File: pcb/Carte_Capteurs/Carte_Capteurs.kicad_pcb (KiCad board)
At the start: 2 copper layers, 129.9 x 60 mm, 0 parts

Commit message: demarrage carte capteurs
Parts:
- added Logo1: LOGO, Insa:insa-image, F.Cu at (210.3, 88.9)
- added U1: FRDM-KL25Z, Insa:FRDM-KL25Z, B.Cu at (149.9, 104.1)

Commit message: version d'echange
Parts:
- added C1: 100nF, Capacitor_SMD:C_1206_3216Metric_Pad1.42x1.75mm_HandSolder, F.Cu at (131.2, 88.8)
- added C2: 100µF, Capacitor_THT:CP_Radial_D6.3mm_P2.50mm, F.Cu at (173.0, 110.4)
- added C3: 100µF, Capacitor_THT:CP_Radial_D6.3mm_P2.50mm, F.Cu at (180.0, 110.4)
- added C4: 100nF, Capacitor_SMD:C_1206_3216Metric_Pad1.42x1.75mm_HandSolder, F.Cu at (131.2, 91.1)
- added D1: LED, LED_THT:LED_D3.0mm, F.Cu at (140.9, 116.2)
- added J10: Conn_01x05, Connector_PinHeader_2.54mm:PinHeader_1x05_P2.54mm_Horizontal, F.Cu at (160.1, 94.5)
- added J11: Conn_01x04, Connector_PinHeader_2.54mm:PinHeader_1x04_P2.54mm_Horizontal, F.Cu at (147.7, 108.3)
- added J12: Conn_01x04, Connector_PinHeader_2.54mm:PinHeader_1x04_P2.54mm_Horizontal, F.Cu at (160.1, 108.3)
- added J5: Conn_02x07_Odd_Even, Connector_PinHeader_2.54mm:PinHeader_2x07_P2.54mm_Vertical, F.Cu at (141.5, 94.5)
- added J6: Molex KK 254, Connector_Molex:Molex_KK-254_AE-6410-04A_1x04_P2.54mm_Vertical, F.Cu at (172.5, 96.2)
- added J7: Samtec FTS-105-01-L-DV, Connector_PinHeader_1.27mm:PinHeader_2x05_P1.27mm_Vertical, F.Cu at (172.3, 100.7)
- added J8: Samtec FTS-105-01-L-DV, Connector_PinHeader_1.27mm:PinHeader_2x05_P1.27mm_Vertical, F.Cu at (176.8, 100.7)
- added J9: Conn_01x05, Connector_PinHeader_2.54mm:PinHeader_1x05_P2.54mm_Horizontal, F.Cu at (147.7, 94.5)
- added R1: R, Resistor_SMD:R_1206_3216Metric_Pad1.42x1.75mm_HandSolder, F.Cu at (142.2, 112.8)
- added U2: XBee, Insa:Xbee3, F.Cu at (116.1, 101.7)
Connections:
- U1 pad 3.16: (no net) -> +BATT
- U1 pad 3.4: (no net) -> /PWR_LED

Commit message: sauvegarde intermediaire
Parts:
- added C10: 100nF, Capacitor_SMD:C_1206_3216Metric_Pad1.42x1.75mm_HandSolder, F.Cu at (108.0, 113.7)
- added C11: 100nF, Capacitor_SMD:C_1206_3216Metric_Pad1.42x1.75mm_HandSolder, F.Cu at (197.5, 113.7)
- added C5: 100nF, Capacitor_SMD:C_1206_3216Metric_Pad1.42x1.75mm_HandSolder, F.Cu at (184.2, 85.1)
- added C6: 100nF, Capacitor_SMD:C_1206_3216Metric_Pad1.42x1.75mm_HandSolder, F.Cu at (123.2, 97.8)
- added C7: 100nF, Capacitor_SMD:C_1206_3216Metric_Pad1.42x1.75mm_HandSolder, F.Cu at (123.2, 90.4)
- added C8: 100nF, Capacitor_SMD:C_1206_3216Metric_Pad1.42x1.75mm_HandSolder, F.Cu at (118.7, 80.0)
- added C9: 100nF, Capacitor_SMD:C_1206_3216Metric_Pad1.42x1.75mm_HandSolder, F.Cu at (131.4, 80.0)
- added J13: Conn_01x02, Connector_PinHeader_2.54mm:PinHeader_1x02_P2.54mm_Vertical, F.Cu at (115.6, 106.7)
- added Q1: NTR3C21NZT1G, Package_TO_SOT_SMD:SOT-23, F.Cu at (119.4, 111.8)
- added R3: 10K, Resistor_SMD:R_1206_3216Metric_Pad1.42x1.75mm_HandSolder, F.Cu at (109.9, 90.2)
- added R4: 10K, Resistor_SMD:R_1206_3216Metric_Pad1.42x1.75mm_HandSolder, F.Cu at (107.3, 100.3)
- added R5: 100R, Resistor_SMD:R_1206_3216Metric_Pad1.42x1.75mm_HandSolder, F.Cu at (123.2, 111.1)
- added RN1: 100R, Resistor_SMD:R_Array_Convex_4x1206, F.Cu at (142.2, 86.4)
- added RN2: 100R, Resistor_SMD:R_Array_Convex_4x1206, F.Cu at (142.2, 94.0)
- added RN3: 10K, Resistor_SMD:R_Array_Convex_4x1206, F.Cu at (167.6, 84.2)
- added SW1: SMR8016C-1, Insa:Nidec_Copal_SMR-8016C, F.Cu at (167.6, 92.1)
- added SW2: Reset, Button_Switch_THT:SW_PUSH_6mm_H4.3mm, F.Cu at (108.6, 83.2)
- added SW3: USER1, Button_Switch_THT:SW_PUSH_6mm_H4.3mm, F.Cu at (106.0, 93.3)
- added SW4: USER2, Button_Switch_THT:SW_PUSH_6mm_H4.3mm, F.Cu at (103.5, 103.5)
- added U3: HDSP-7501, Display_7Segment:HDSP-A151, F.Cu at (156.8, 94.6)
- added U4: TCL6C598, Package_SO:TSSOP-16_4.4x5mm_P0.65mm, F.Cu at (134.6, 92.7)
- J10, J9: value Conn_01x05 -> DF3A-5P-2DS; footprint Connector_PinHeader_2.54mm:PinHeader_1x05_P2.54mm_Horizontal -> Insa:DF3A-5P-2DS
- J11, J12: value Conn_01x04 -> DF3A-4P-2DS; footprint Connector_PinHeader_2.54mm:PinHeader_1x04_P2.54mm_Horizontal -> Insa:DF3A-4P-2DS
- moved Logo1 116.4 mm to (96.4, 113.0), turned to 270 degrees
- moved U2 77.0 mm to (190.5, 81.9)
- moved C4 73.5 mm to (203.2, 105.8), turned to 270 degrees
- moved C1 63.2 mm to (185.4, 121.3), turned to 180 degrees
- moved J8 57.3 mm to (119.6, 97.2), turned to 270 degrees
- moved J7 53.8 mm to (119.6, 89.8), turned to 270 degrees
- moved J9 46.8 mm to (107.3, 118.1)
- moved J11 44.2 mm to (118.1, 75.6), turned to 180 degrees
- moved J12 44.0 mm to (130.8, 75.6), turned to 180 degrees
- moved J10 43.6 mm to (196.8, 118.1)
- moved C3 18.4 mm to (197.5, 104.8), turned to 270 degrees
- moved C2 14.6 mm to (186.7, 115.6), turned to 180 degrees
- moved J5 14.6 mm to (145.4, 108.6), turned to 90 degrees
- moved J6 14.4 mm to (181.6, 107.3)
- moved D1 12.5 mm to (130.8, 108.7), turned to 90 degrees
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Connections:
- J10 pad 1: (no net) -> /ENC_INDEX2
- J10 pad 2: (no net) -> +3V3
- J10 pad 3: (no net) -> /ENC_SIG_A2
- J10 pad 4: (no net) -> /ENC_SIG_B2
- J10 pad 5: (no net) -> GND
- J11 pad 1: (no net) -> +3V3
- J11 pad 2: (no net) -> /SENS_SDA1
- J11 pad 3: (no net) -> GND
- J11 pad 4: (no net) -> /SENS_SCL1
- J12 pad 1: (no net) -> +3V3
- J12 pad 2: (no net) -> /SENS_SDA2
- J12 pad 3: (no net) -> GND
- J12 pad 4: (no net) -> /SENS_SCL2
- J5 pad 1: (no net) -> /DISABLE_MOT_R
- J5 pad 10: (no net) -> /PWM_MOT_R_2
- J5 pad 12: (no net) -> /PWM_MOT_L_1
- J5 pad 14: (no net) -> /PWM_MOT_L_2
- J5 pad 2: (no net) -> /SERVO_PWM
- J5 pad 3: (no net) -> /DISABLE_MOT_L
- J5 pad 4: (no net) -> /FEEDBACK_MOT_R
- J5 pad 6: (no net) -> /FEEDBACK_MOT_L
- J5 pad 8: (no net) -> /PWM_MOT_R_1
- J7 pad 1: (no net) -> GND
- J7 pad 10: (no net) -> GND
- J7 pad 2: (no net) -> /CCD_AD0
- J7 pad 3: (no net) -> GND
- J7 pad 4: (no net) -> /CCD_SI0
- J7 pad 5: (no net) -> GND
- J7 pad 6: (no net) -> /CCD_CLK0
- J7 pad 7: (no net) -> GND
- J7 pad 8: (no net) -> +3V3
- J7 pad 9: (no net) -> GND
- J8 pad 1: (no net) -> GND
- J8 pad 10: (no net) -> GND
- J8 pad 2: (no net) -> /CCD_AD1
- J8 pad 3: (no net) -> GND
- J8 pad 4: (no net) -> /CCD_SI1
- J8 pad 5: (no net) -> GND
- J8 pad 6: (no net) -> /CCD_CLK1
- J8 pad 7: (no net) -> GND
- J8 pad 8: (no net) -> +3V3
- J8 pad 9: (no net) -> GND
- J9 pad 1: (no net) -> /ENC_INDEX1
- J9 pad 2: (no net) -> +3V3
- J9 pad 3: (no net) -> /ENC_SIG_A1
- J9 pad 4: (no net) -> /ENC_SIG_B1
- J9 pad 5: (no net) -> GND
- U1 pad 1.1: (no net) -> /DISABLE_MOT_R
- U1 pad 1.10: (no net) -> /PWM_MOT_R_1
- U1 pad 1.11: (no net) -> /DISP_SIN
- U1 pad 1.12: (no net) -> /PWM_MOT_R_2
- U1 pad 1.13: (no net) -> /DISP_LATCH
- U1 pad 1.14: (no net) -> /PWM_MOT_L_1
- U1 pad 1.16: (no net) -> /PWM_MOT_L_2
- U1 pad 1.2: (no net) -> /ENC_SIG_B1
- U1 pad 1.3: (no net) -> /DISABLE_MOT_L
- U1 pad 1.4: (no net) -> /ENC_SIG_B2
- U1 pad 1.6: (no net) -> /ENC_INDEX1
- U1 pad 1.8: (no net) -> /SERVO_PWM
- U1 pad 1.9: (no net) -> /DISP_CLK
- U1 pad 2.1: (no net) -> /CAM_LED
- U1 pad 2.10: (no net) -> /SW_USER1
- U1 pad 2.12: (no net) -> /SW_USER2
- U1 pad 2.14: (no net) -> GND
- U1 pad 2.17: (no net) -> /FEEDBACK_MOT_L
- U1 pad 2.18: (no net) -> /SENS_SCL1
- U1 pad 2.2: (no net) -> /ENC_INDEX2
- U1 pad 2.20: (no net) -> /SENS_SDA1
- U1 pad 2.4: (no net) -> /FEEDBACK_MOT_R
- U1 pad 3.1: (no net) -> /CCD_SI0
- U1 pad 3.11: (no net) -> /ROT_SW_2
- U1 pad 3.12: (no net) -> GND
- U1 pad 3.13: (no net) -> /ROT_SW_4
- U1 pad 3.14: (no net) -> GND
- U1 pad 3.15: (no net) -> /ROT_SW_8
- U1 pad 3.3: (no net) -> /CCD_CLK0
- U1 pad 3.5: (no net) -> /CCD_SI1
- U1 pad 3.6: (no net) -> /RESET
- U1 pad 3.7: (no net) -> /CCD_CLK1
- U1 pad 3.9: (no net) -> /ROT_SW_1
- U1 pad 4.10: (no net) -> /CCD_AD0
- U1 pad 4.12: (no net) -> /CCD_AD1
- U1 pad 4.2: (no net) -> /SENS_SCL2
- U1 pad 4.4: (no net) -> /SENS_SDA2
- U1 pad 4.5: (no net) -> /USART_TX
- U1 pad 4.6: (no net) -> /ENC_SIG_A1
- U1 pad 4.7: (no net) -> /USART_RX
- U1 pad 4.8: (no net) -> /ENC_SIG_A2
- U2 pad 2: (no net) -> /USART_RX
- U2 pad 3: (no net) -> /USART_TX
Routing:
- net GND: track 0.00 -> 341.3 mm
- net +3V3: track 0.00 -> 227.5 mm, vias 0 -> 3
- net +BATT: track 0.00 -> 100.1 mm
- net /ENC_INDEX1: track 0.00 -> 77.9 mm, vias 0 -> 1
- net /ENC_SIG_B1: track 0.00 -> 77.1 mm, vias 0 -> 1
- net /ENC_INDEX2: track 0.00 -> 52.3 mm
- net /DISABLE_MOT_R: track 0.00 -> 44.9 mm, vias 0 -> 2
- net /PWM_MOT_L_1: track 0.00 -> 37.3 mm, vias 0 -> 1
- net /PWM_MOT_L_2: track 0.00 -> 36.3 mm
- net /ENC_SIG_B2: track 0.00 -> 35.9 mm
- net /DISABLE_MOT_L: track 0.00 -> 34.1 mm, vias 0 -> 1
- net /SERVO_PWM: track 0.00 -> 33.4 mm, vias 0 -> 1
- net Net-(RN2-Pad2): track 0.00 -> 27.0 mm, vias 0 -> 1
- net /PWM_MOT_R_1: track 0.00 -> 26.7 mm
- net /ROT_SW_2: track 0.00 -> 25.0 mm
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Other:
- outline, holes or cut-outs redrawn
- net class Default: trace_width 0.25 -> 0.35; via_dia 0.8 -> 0.7
- net class Power added: clearance 0.2, trace_width 0.5, via_dia 1, via_drill 0.6

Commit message: Cartes terminées
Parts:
- added R6: 4.7K, Resistor_SMD:R_1206_3216Metric_Pad1.42x1.75mm_HandSolder, B.Cu at (132.1, 73.0)
- added R7: 4.7K, Resistor_SMD:R_1206_3216Metric_Pad1.42x1.75mm_HandSolder, B.Cu at (132.1, 70.5)
- added R8: 4.7K, Resistor_SMD:R_1206_3216Metric_Pad1.42x1.75mm_HandSolder, F.Cu at (127.6, 97.8)
- added R9: 4.7K, Resistor_SMD:R_1206_3216Metric_Pad1.42x1.75mm_HandSolder, F.Cu at (127.6, 90.2)
- added Sym1: Symbol_CreativeCommons_CopperTop_Type2_Small, Symbol:Symbol_CreativeCommons_CopperTop_Type2_Small, F.Cu at (189.1, 92.7)
- added Sym2: Symbol_CC-Attribution_CopperTop_Small, Symbol:Symbol_CC-Attribution_CopperTop_Small, F.Cu at (189.1, 85.7)
- added Sym3: Symbol_CC-ShareAlike_CopperTop_Small, Symbol:Symbol_CC-ShareAlike_CopperTop_Small, F.Cu at (189.1, 78.7)
- added Sym4: OSHW-Logo2_9.8x8mm_SilkScreen, Symbol:OSHW-Logo2_9.8x8mm_SilkScreen, F.Cu at (173.4, 102.9)
- added Sym6: WEEE-Logo_5.6x8mm_SilkScreen, Symbol:WEEE-Logo_5.6x8mm_SilkScreen, F.Cu at (120.0, 120.0)
- added Sym7: ESD-Logo_6.6x6mm_SilkScreen, Symbol:ESD-Logo_6.6x6mm_SilkScreen, F.Cu at (113.0, 83.2)
- J5: footprint Connector_PinHeader_2.54mm:PinHeader_2x07_P2.54mm_Vertical -> Connector_Multicomp:Multicomp_MC9A12-1434_2x07_P2.54mm_Vertical
- moved C5 8.25 mm to (175.9, 85.1)
- moved J8 5.46 mm to (114.3, 98.4), turned to 90 degrees
- moved J7 5.41 mm to (114.3, 90.8), turned to 90 degrees
- turned C6 to 270 degrees
- turned C7 to 270 degrees
- turned J5 to 0 degrees
- renumbered Logo1 to Sym5
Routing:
- net /ENC_SIG_A1: track 0.00 -> 136.2 mm, vias 0 -> 2
- net /CCD_AD1: track 0.00 -> 112.0 mm, vias 0 -> 4
- net /CCD_AD0: track 0.00 -> 83.6 mm, vias 0 -> 2
- net /SW_USER1: track 10.4 -> 91.9 mm
- net /ENC_SIG_A2: track 0.00 -> 77.2 mm
- net +BATT: track 100.1 -> 175.5 mm, vias 0 -> 3
- net /DISP_SIN: track 2.39 -> 70.8 mm, vias 0 -> 3
- net /SW_USER2: track 10.4 -> 77.9 mm
- net /SENS_SCL1: track 0.00 -> 65.3 mm, vias 0 -> 2
- net GND: track 341.3 -> 406.3 mm, vias 0 -> 4
- net /SENS_SDA1: track 0.00 -> 63.9 mm, vias 0 -> 1
- net /SENS_SCL2: track 0.00 -> 57.8 mm
- net +3V3: track 227.5 -> 281.1 mm, vias 3 -> 4
- net /DISP_CLK: track 3.02 -> 56.5 mm, vias 0 -> 3
- net /CCD_CLK1: track 0.00 -> 51.2 mm
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- added copper zone on B.Cu, net GND
- added copper zone on F.Cu, net GND
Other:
- board text added: "Toulouse"

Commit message: ajout des versions sur les cartes
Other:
- board text added: "1"
- board text added: "2"
- board text added: "Rev 1A"
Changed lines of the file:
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@@
   (general
     (thickness 1.6)
-    (drawings 18)
+    (drawings 21)
     (tracks 735)
     (zones 0)
@@
     )
   )
+  (gr_text "Rev 1A" (at 207.645 114.935) (layer F.SilkS)
+    (effects (font (size 1 1) (thickness 0.15)))
+  )
+  (gr_text 2 (at 103.505 68.58) (layer B.Cu)
+    (effects (font (size 1.5 1.5) (thickness 0.3)) (justify mirror))
+  )
+  (gr_text 1 (at 103.505 68.58) (layer F.Cu)
+    (effects (font (size 1.5 1.5) (thickness 0.3)))
+  )
   (gr_poly (pts (xy 186.182 75.946) (xy 192.024 75.946) (xy 192.024 95.504) (xy 186.182 95.504)) (layer F.Mask) (width 0.1))

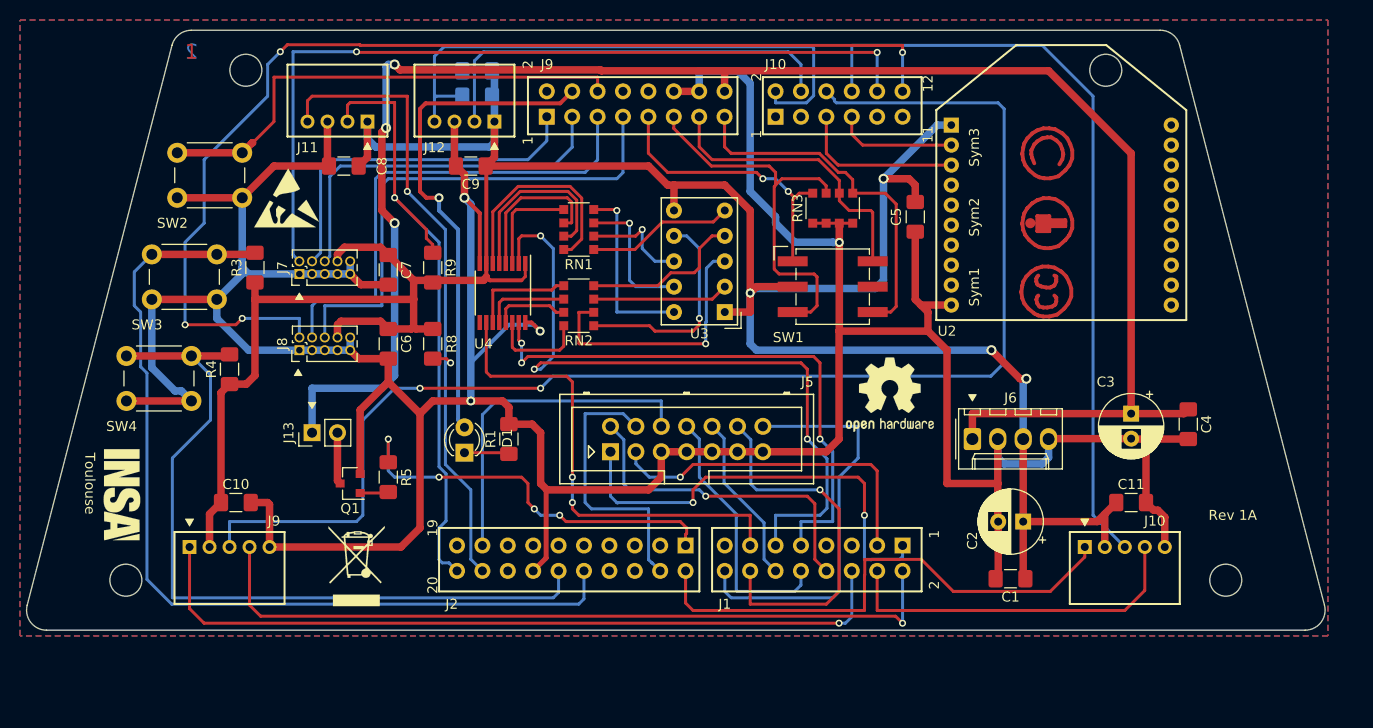
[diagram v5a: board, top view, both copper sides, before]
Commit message: Correction sur carte capteur + realisation des pieces du circuit sous LibreCad/InkScape
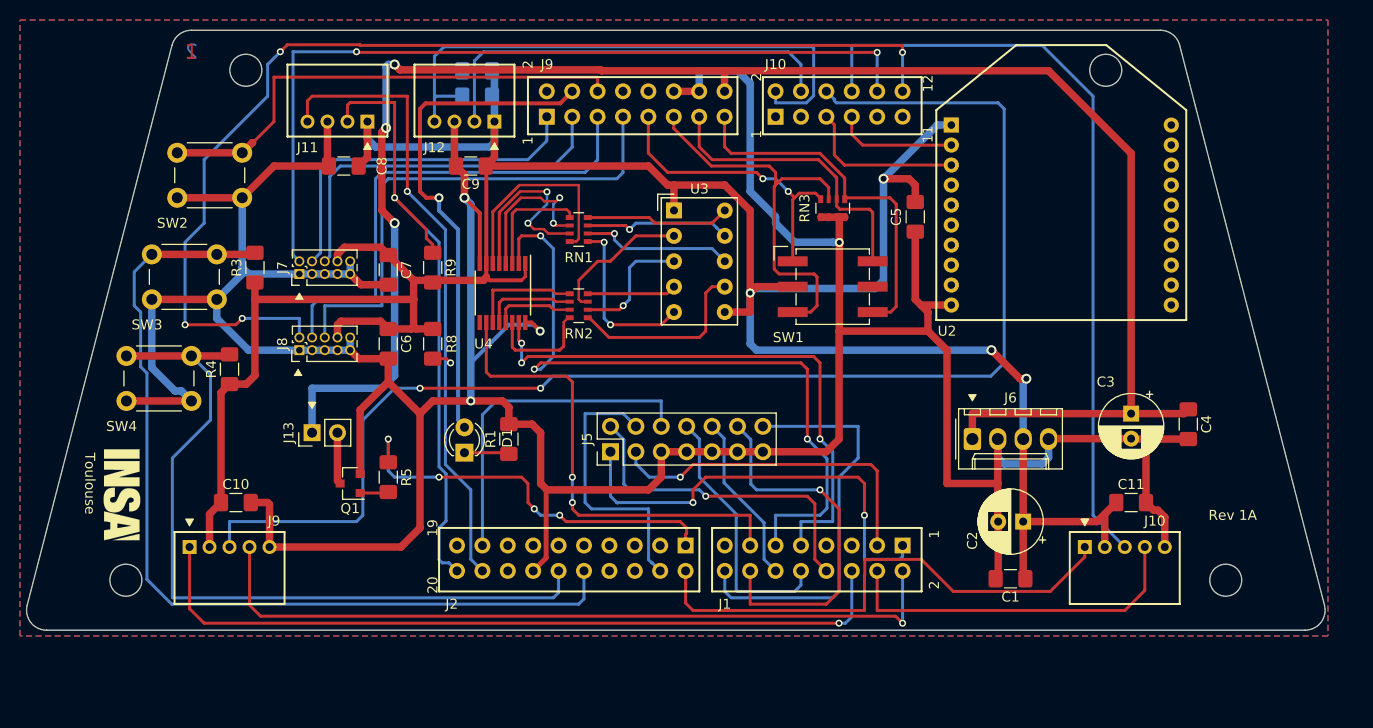
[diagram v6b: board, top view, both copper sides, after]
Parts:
- removed Sym1: Symbol_CreativeCommons_CopperTop_Type2_Small, Symbol:Symbol_CreativeCommons_CopperTop_Type2_Small
- removed Sym2: Symbol_CC-Attribution_CopperTop_Small, Symbol:Symbol_CC-Attribution_CopperTop_Small
- removed Sym3: Symbol_CC-ShareAlike_CopperTop_Small, Symbol:Symbol_CC-ShareAlike_CopperTop_Small
- removed Sym4: OSHW-Logo2_9.8x8mm_SilkScreen, Symbol:OSHW-Logo2_9.8x8mm_SilkScreen
- removed Sym6: WEEE-Logo_5.6x8mm_SilkScreen, Symbol:WEEE-Logo_5.6x8mm_SilkScreen
- removed Sym7: ESD-Logo_6.6x6mm_SilkScreen, Symbol:ESD-Logo_6.6x6mm_SilkScreen
- J5: footprint Connector_Multicomp:Multicomp_MC9A12-1434_2x07_P2.54mm_Vertical -> Connector_PinHeader_2.54mm:PinHeader_2x07_P2.54mm_Vertical
- RN1, RN2: value 100R -> 220R; footprint Resistor_SMD:R_Array_Convex_4x1206 -> Resistor_SMD:R_Array_Convex_4x0603
- RN3: footprint Resistor_SMD:R_Array_Convex_4x1206 -> Resistor_SMD:R_Array_Convex_4x0603
- moved U3 11.4 mm to (151.8, 84.5), turned to 0 degrees
- turned J5 to 90 degrees
- renumbered Sym5 to Logo1
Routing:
- net Net-(RN2-Pad2): track 27.0 -> 12.5 mm
- net Net-(RN2-Pad4): track 16.3 -> 8.92 mm
- net Net-(RN1-Pad2): track 10.7 -> 15.2 mm
- net Net-(RN1-Pad4): track 18.2 -> 14.5 mm, vias 1 -> 0
- net Net-(RN2-Pad1): track 21.7 -> 18.9 mm, vias 1 -> 0
- net Net-(RN1-Pad1): track 14.7 -> 17.1 mm, vias 0 -> 2
- net Net-(RN1-Pad5): track 10.3 -> 11.5 mm
- net Net-(RN2-Pad8): track 9.94 -> 11.1 mm
- net /ROT_SW_1: track 28.5 -> 29.6 mm
- net GND: track 406.3 -> 405.3 mm
- net /ROT_SW_2: track 39.4 -> 40.2 mm
- net Net-(RN2-Pad6): track 8.58 -> 9.32 mm
- net Net-(RN1-Pad7): track 18.7 -> 19.3 mm, vias 0 -> 2
- net Net-(RN1-Pad8): track 21.9 -> 21.3 mm
- net Net-(RN2-Pad3): track 13.6 -> 14.3 mm
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
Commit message: correction sur carte capteur
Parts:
- added R10: 4.7K, Resistor_SMD:R_1206_3216Metric_Pad1.42x1.75mm_HandSolder, F.Cu at (187.3, 72.4)
- added R11: 2.2K, Resistor_SMD:R_1206_3216Metric_Pad1.42x1.75mm_HandSolder, F.Cu at (187.3, 79.4)
- R1: value R -> 100R
- moved C7 2.55 mm to (125.7, 90.2)
- moved C6 2.54 mm to (125.7, 97.8)
- moved R8 1.27 mm to (128.9, 97.8)
- moved R9 1.27 mm to (128.9, 90.2)
- moved R3 0.64 mm to (109.2, 90.2)
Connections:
- J5 pad 1: /DISABLE_MOT_R -> /DISABLE_MOT_L
- J5 pad 10: /PWM_MOT_R_2 -> /FEEDBACK_MOT_R
- J5 pad 12: /PWM_MOT_L_1 -> /PWM_MOT_R_1
- J5 pad 14: /PWM_MOT_L_2 -> /PWM_MOT_R_2
- J5 pad 3: /DISABLE_MOT_L -> /DISABLE_MOT_R
- J5 pad 4: /FEEDBACK_MOT_R -> /FEEDBACK_MOT_L
- J5 pad 6: /FEEDBACK_MOT_L -> /PWM_MOT_L_1
- J5 pad 8: /PWM_MOT_R_1 -> /PWM_MOT_L_2
- U1 pad 4.1: (no net) -> /USART_TX
- U1 pad 4.3: (no net) -> /USART_RX
- U1 pad 4.5: /USART_TX -> /VBAT_ADC
- U1 pad 4.7: /USART_RX -> (no net)
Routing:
- net /VBAT_ADC: track 0.00 -> 24.9 mm
- net /PWM_MOT_L_2: track 40.8 -> 16.1 mm
- net GND: track 405.3 -> 429.7 mm
- net /PWM_MOT_L_1: track 37.3 -> 51.1 mm
- net /FEEDBACK_MOT_R: track 27.8 -> 41.4 mm, vias 0 -> 1
- net /DISABLE_MOT_R: track 44.9 -> 36.4 mm
- net /USART_RX: track 12.2 -> 17.2 mm
- net /USART_TX: track 16.3 -> 21.0 mm
- net /SERVO_PWM: track 33.4 -> 38.1 mm
- net +3V3: track 281.1 -> 285.2 mm
- net /DISABLE_MOT_L: track 34.1 -> 38.0 mm
- net /FEEDBACK_MOT_L: track 34.1 -> 30.8 mm
- net /PWM_MOT_R_2: track 17.1 -> 19.6 mm
- net /SENS_SCL1: track 65.3 -> 66.4 mm
- net /PWM_MOT_R_1: track 26.7 -> 25.7 mm
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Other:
- board text added: "Rev 2A"
- board text removed: "Rev 1A"

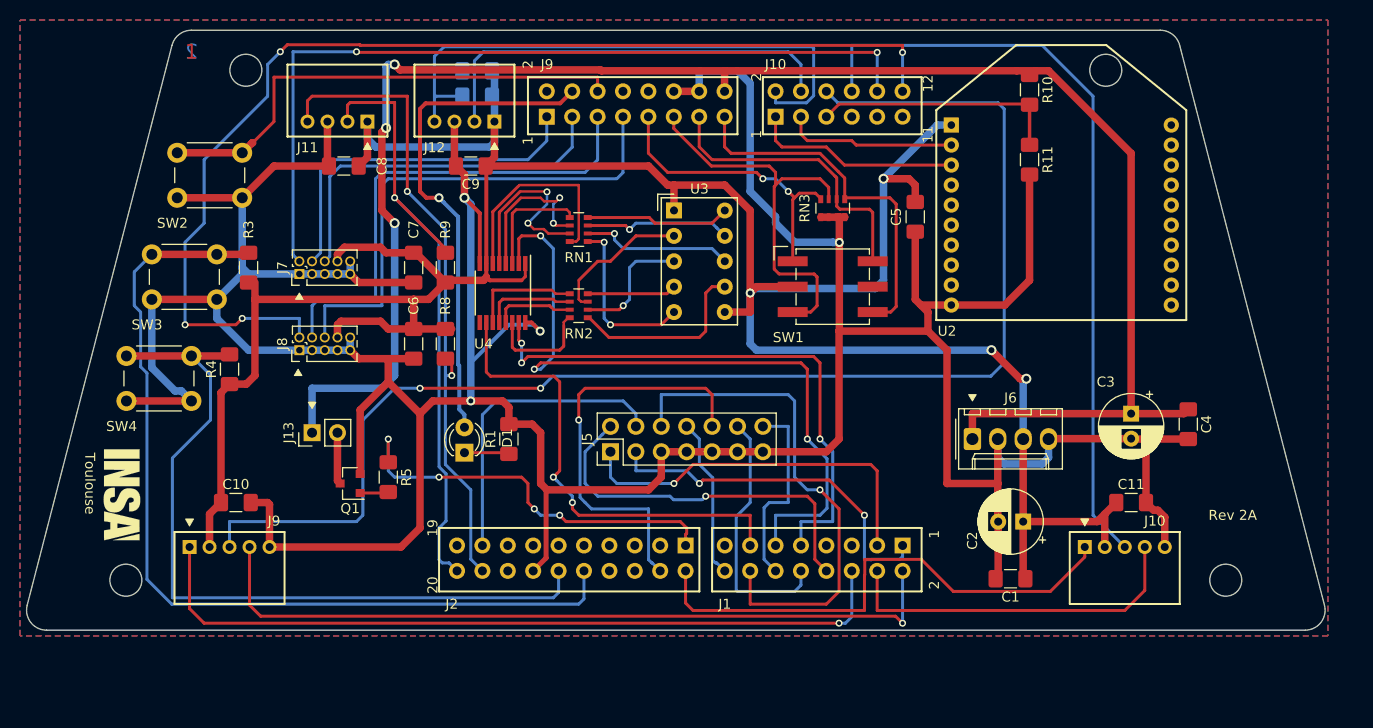
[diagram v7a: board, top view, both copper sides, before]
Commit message: creation d'une carte camera et d'une carte pour els led
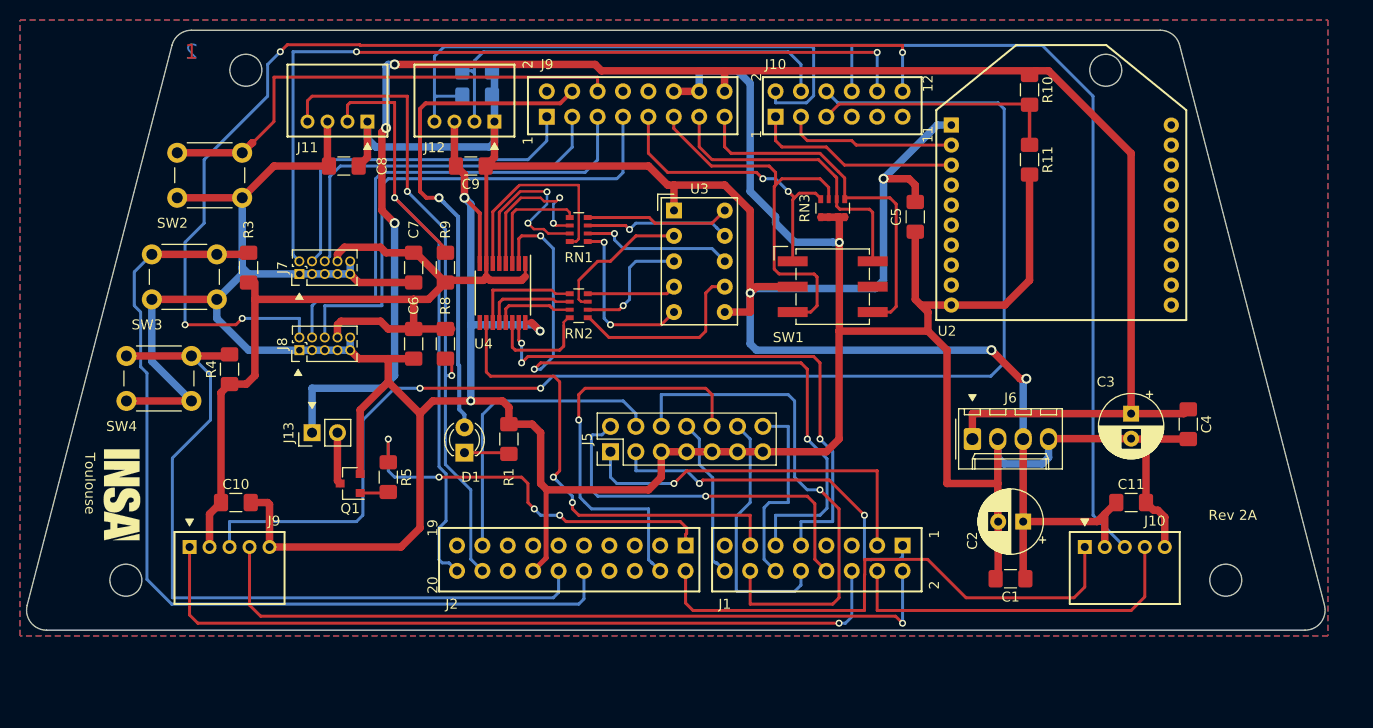
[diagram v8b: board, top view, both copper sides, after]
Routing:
- net /ENC_INDEX2: track 52.3 -> 54.6 mm
- net GND: track 429.7 -> 431.6 mm
- net /DISABLE_MOT_L: track 38.0 -> 37.5 mm
